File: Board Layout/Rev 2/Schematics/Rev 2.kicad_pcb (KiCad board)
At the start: 2 copper layers, 12 parts, among them P1 CONN_1, P2 CONN_1, P3 CONN_1, Q1 NPN, Q2 NPN, Q3 NPN

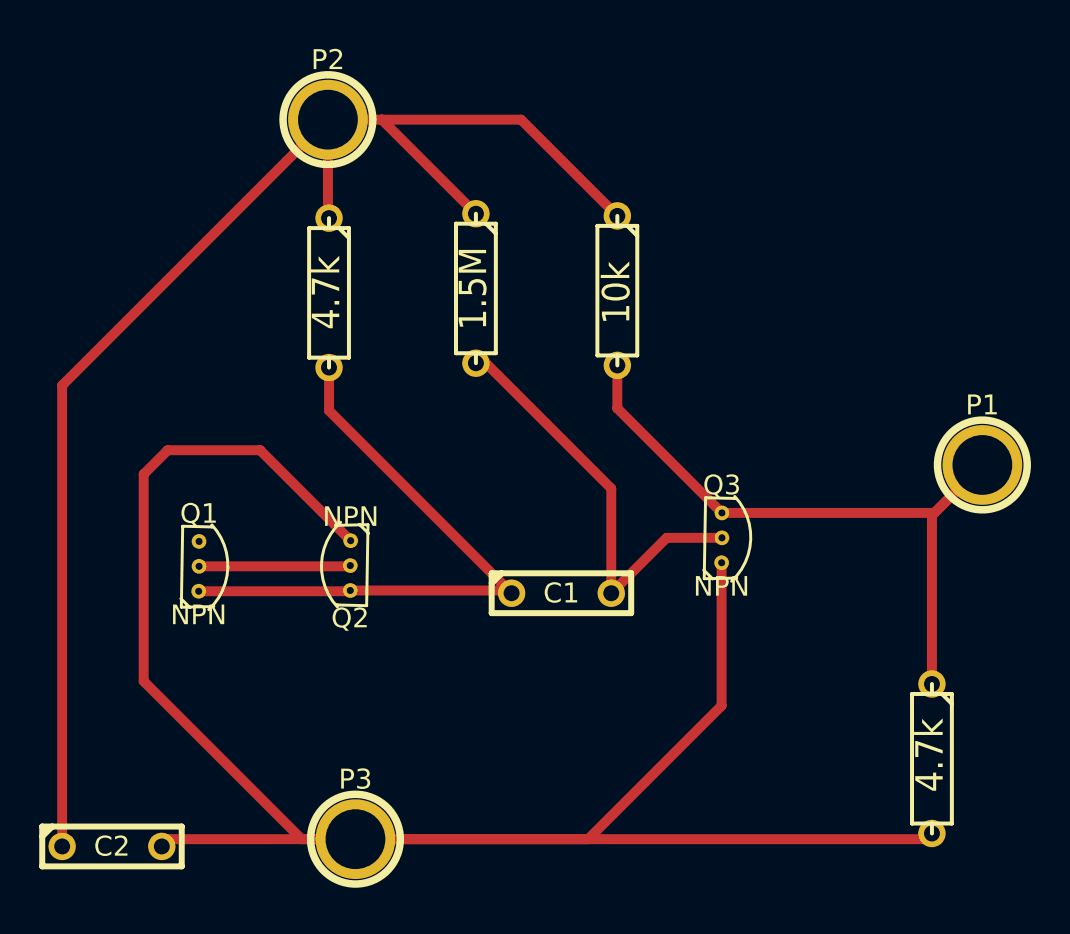
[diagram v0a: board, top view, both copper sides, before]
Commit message: Board Completion
RNG is complete, -  Trace widths much larger, condusive to self etching.
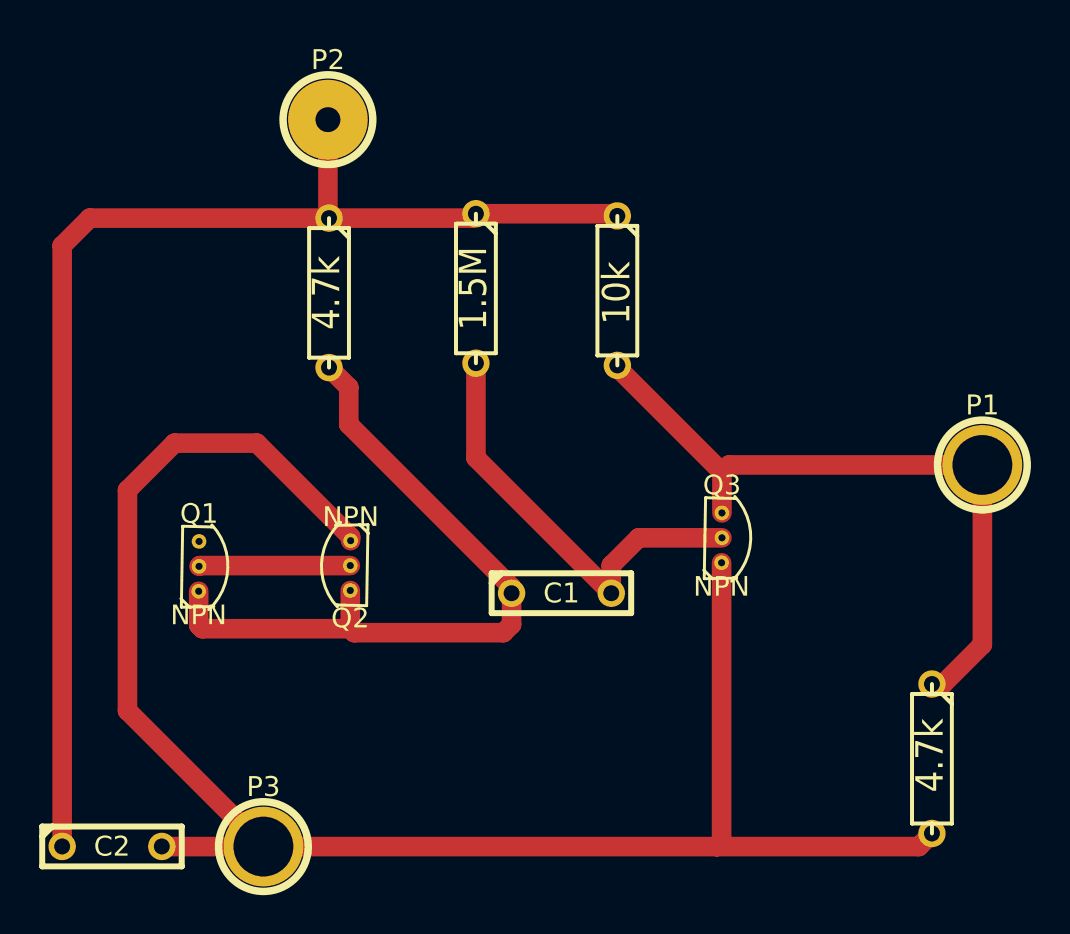
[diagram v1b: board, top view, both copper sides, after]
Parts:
- moved P3 4.71 mm to (192.0, 173.3)
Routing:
- net N-000001: track 106.0 -> 89.7 mm
- net N-000007: track 71.3 -> 64.7 mm
- net N-000003: track 31.4 -> 36.9 mm
- net N-000004: track 21.7 -> 22.2 mm
- net N-000006: track 36.2 -> 35.7 mm
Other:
- net class Default: trace_width 0.508 -> 1
- net class Large added: clearance 0.254, trace_width 1, via_dia 0.889, via_drill 0.635
